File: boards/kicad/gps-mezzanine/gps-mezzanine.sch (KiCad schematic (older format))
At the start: 13 parts, among them P1 CONN_02X20, Q1 BSS138, Q2 BSS138, U1 MCP1700T-3302E/TT, U2 FGPMMOPA6H

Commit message: Update GPS mezzanine
Adds CR2032 backup battery.
Adds uFL external antenna connector.
Connects PPS and fix signal to base board.
Switches to TXS0104 for level translation.

Signed-off-by: Michael Welling <mwelling@ieee.org>
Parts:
- removed Q1, Q2: BSS138, TO_SOT_Packages_SMD:SOT-23, symbol BSS138
- removed R2, R4: 10K, Resistors_SMD:R_0603, symbol R
- added BT1: Battery_Cell, 96boards:BAT-HLD-001, symbol Battery_Cell
- added C4, C5: .1uF, Capacitors_SMD:C_0603, symbol C_Small
- added JK1: uFL, 96boards:U.FL-R-SMT-1, symbol ANTENNA_RCPT
- added MH1, MH2, MH3, MH4: M2.5, Mounting_Holes:MountingHole_2-5mm, symbol MOUNTING_HOLE
- added U3: TXS0104E, Housings_SSOP:SSOP-14_5.3x6.2mm_Pitch0.65mm, symbol TXS0104E
- R1: value 10K -> 1K
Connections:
- net labels added: +BATT, GPS_1PPS
- wire segments 81 -> 92
- no-connect marks 4 -> 2
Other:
- note added: "KIT ACCESSORIES:\n1 - CR2032\n2 - M2102-2545-AL\n2 - M2.5 Screws\n2 - M2.4 Nuts"
- moved on the sheet: C2, C3, U1

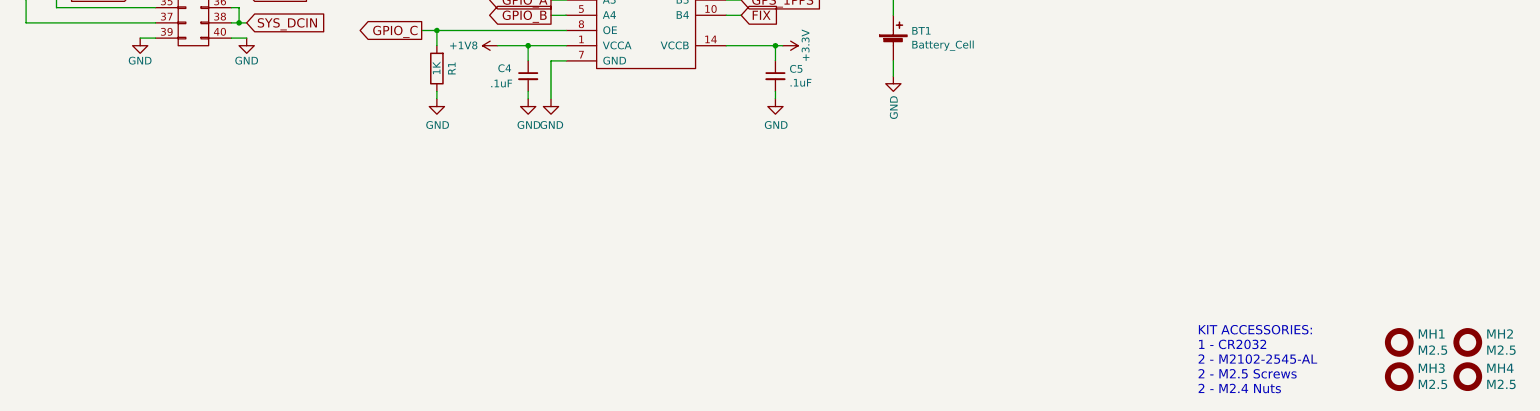
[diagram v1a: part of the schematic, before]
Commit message: Add UART header and schematic PDF
Signed-off-by: Michael Welling <mwelling@ieee.org>
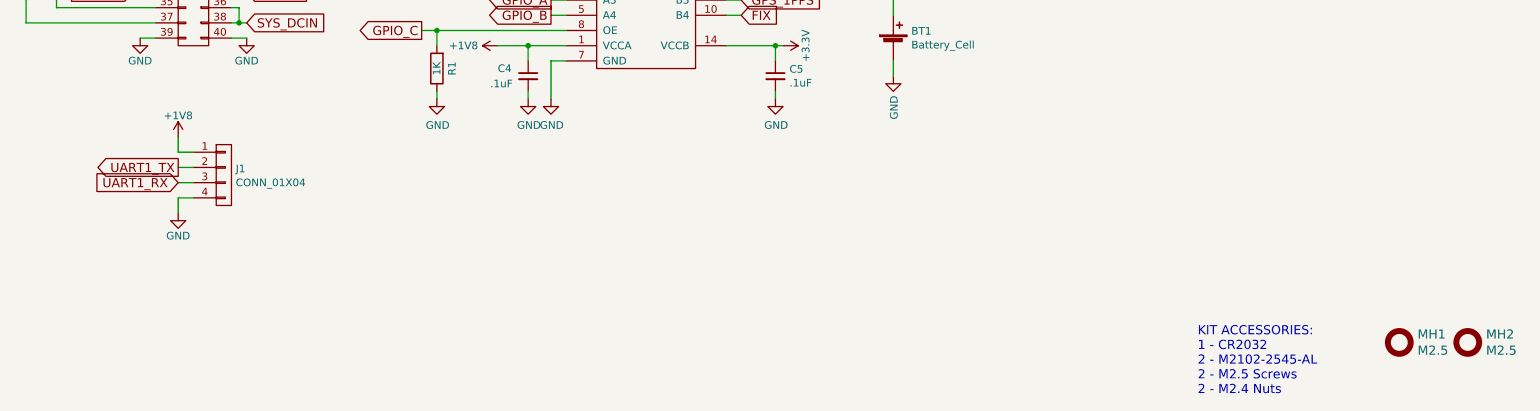
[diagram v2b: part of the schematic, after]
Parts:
- removed MH3, MH4: M2.5, Mounting_Holes:MountingHole_2-5mm, symbol MOUNTING_HOLE
- added J1: CONN_01X04, Pin_Headers:Pin_Header_Straight_1x04, symbol CONN_01X04
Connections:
- net +1V8: now also J1.1 (P1)
- net GND: now also J1.4 (P4)
- net UART1_RX: now also J1.3 (P3)
- net UART1_TX: now also J1.2 (P2)
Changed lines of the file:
@@
-	1    0    0    -1
-$EndComp
-$Comp
-L MOUNTING_HOLE MH3
-U 1 1 5A1BBDB6
-P 10425 6325
-F 0 "MH3" H 10545 6378 60  0000 L CNN
-F 1 "M2.5" H 10545 6272 60  0000 L CNN
-F 2 "Mounting_Holes:MountingHole_2-5mm" H 10425 6325 60  0001 C CNN
-F 3 "" H 10425 6325 60  0001 C CNN
-	1    10425 6325
-	1    0    0    -1
-$EndComp
-$Comp
-L MOUNTING_HOLE MH4
-U 1 1 5A1BBDF8
-P 10875 6325
-F 0 "MH4" H 10995 6378 60  0000 L CNN
-F 1 "M2.5" H 10995 6272 60  0000 L CNN
-F 2 "Mounting_Holes:MountingHole_2-5mm" H 10875 6325 60  0001 C CNN
-F 3 "" H 10875 6325 60  0001 C CNN
-	1    10875 6325
 	1    0    0    -1
 $EndComp
 Text Notes 9100 6450 0    60   ~ 0
 KIT ACCESSORIES:\n1 - CR2032\n2 - M2102-2545-AL\n2 - M2.5 Screws\n2 - M2.4 Nuts
+$Comp
+L GND #PWR030
+U 1 1 5A21B1B9
+P 2400 5250
+F 0 "#PWR030" H 2400 5000 50  0001 C CNN
+F 1 "GND" H 2400 5100 50  0000 C CNN
+F 2 "" H 2400 5250 60  0000 C CNN
+F 3 "" H 2400 5250 60  0000 C CNN
+	1    2400 5250
+	1    0    0    -1
+$EndComp
+Text GLabel 2400 4950 0    60   Output ~ 0
+UART1_TX
+Text GLabel 2400 5050 0    60   Input ~ 0
+UART1_RX
+$Comp
+L CONN_01X04 J1
+U 1 1 5A21B99A
+P 2700 5000
+F 0 "J1" H 2778 5041 50  0000 L CNN
+F 1 "CONN_01X04" H 2778 4950 50  0000 L CNN
+F 2 "Pin_Headers:Pin_Header_Straight_1x04" H 2700 5000 50  0001 C CNN
+F 3 "" H 2700 5000 50  0001 C CNN
+	1    2700 5000
+	1    0    0    -1
+$EndComp
+$Comp
+L +1V8 #PWR029
+U 1 1 5A21BAE7
+P 2400 4750
+F 0 "#PWR029" H 2400 4600 50  0001 C CNN
+F 1 "+1V8" H 2400 4890 50  0000 C CNN
+F 2 "" H 2400 4750 60  0000 C CNN
+F 3 "" H 2400 4750 60  0000 C CNN
+	1    2400 4750
+	1    0    0    -1
+$EndComp
+Wire Wire Line
+	2400 4750 2400 4850
+Wire Wire Line
+	2400 4850 2500 4850
+Wire Wire Line
+	2400 4950 2500 4950
+Wire Wire Line
+	2400 5050 2500 5050
+Wire Wire Line
+	2400 5250 2400 5150
+Wire Wire Line
+	2400 5150 2500 5150
 $EndSCHEMATC

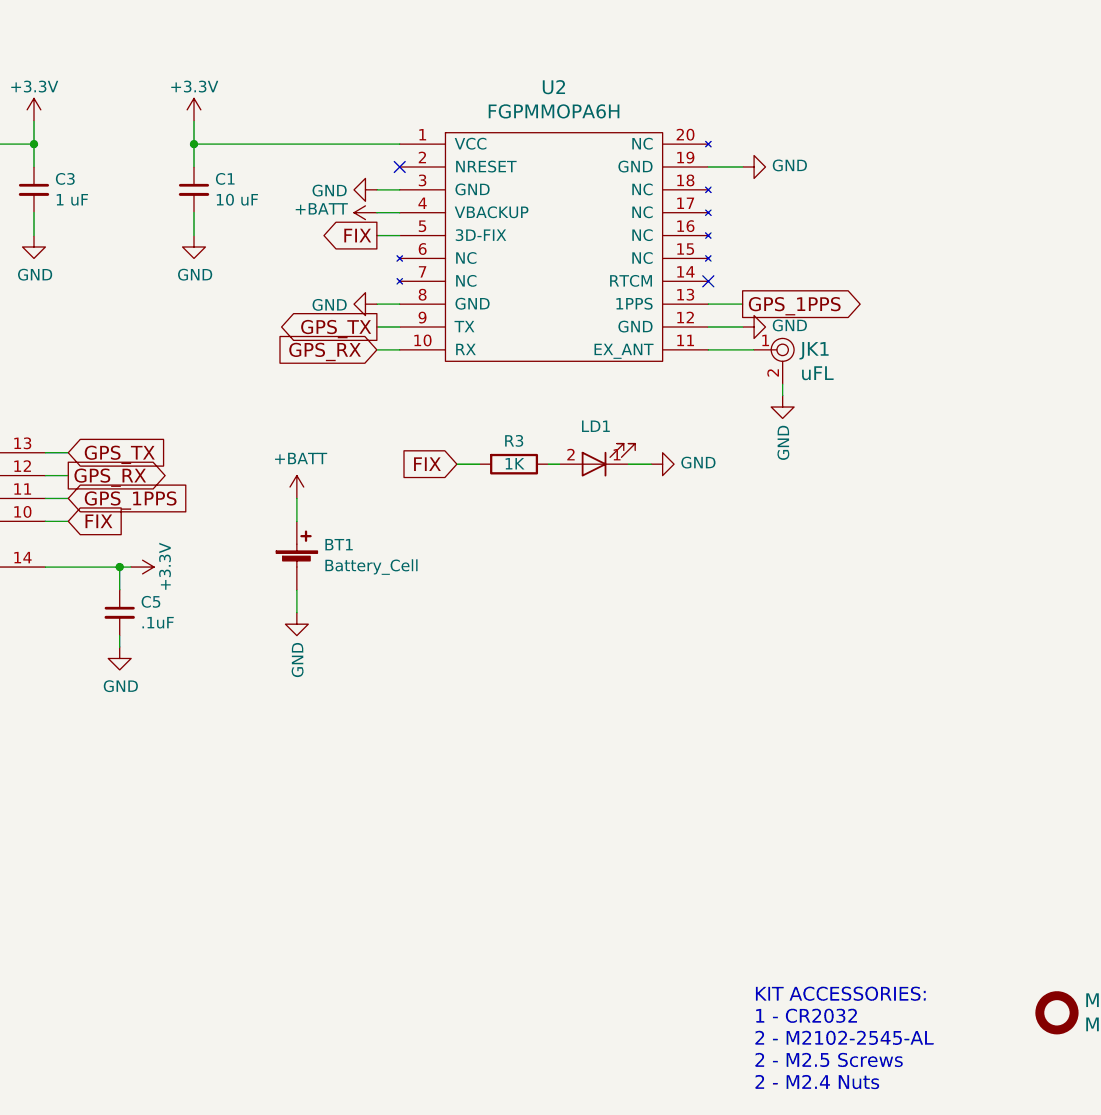
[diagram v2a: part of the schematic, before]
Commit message: Add ferrite bead to GPS power supply
Signed-off-by: Michael Welling <mwelling@ieee.org>
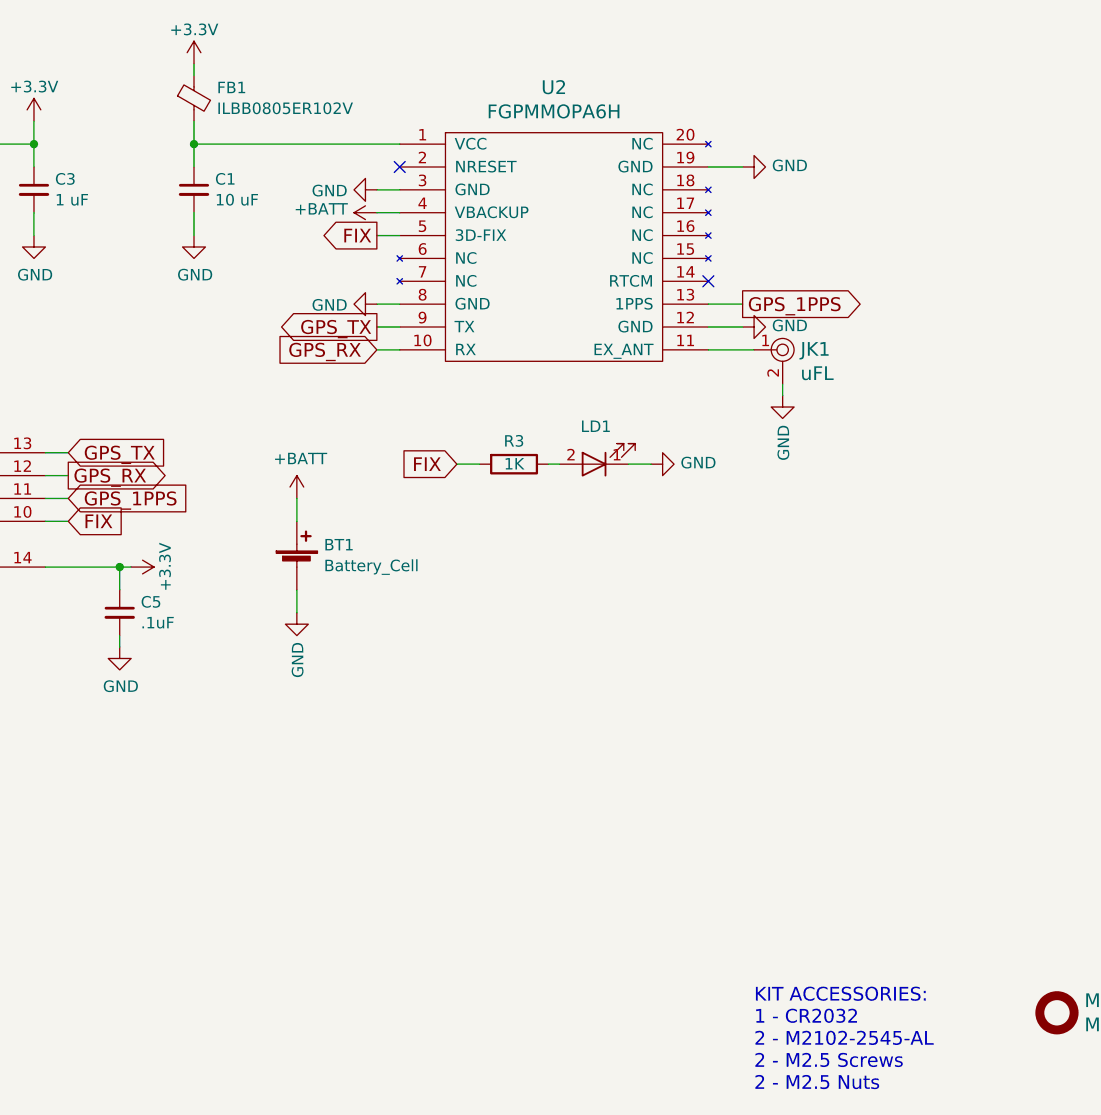
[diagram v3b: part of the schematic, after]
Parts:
- added FB1: ILBB0805ER102V, Resistors_SMD:R_0805_HandSoldering, symbol Ferrite_Bead_Small
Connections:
- net +3V3: now also FB1.1; no longer C1.1, U2.1 (VCC)
- new net: C1.1, FB1.2, U2.1 (VCC)
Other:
- note added: "KIT ACCESSORIES:\n1 - CR2032\n2 - M2102-2545-AL\n2 - M2.5 Screws\n2 - M2.5 Nuts"
- note removed: "KIT ACCESSORIES:\n1 - CR2032\n2 - M2102-2545-AL\n2 - M2.5 Screws\n2 - M2.4 Nuts"
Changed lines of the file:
@@
 L +3.3V #PWR06
 U 1 1 59ACB38D
-P 6650 2200
-F 0 "#PWR06" H 6650 2050 50  0001 C CNN
-F 1 "+3.3V" H 6650 2350 50  0000 C CNN
-F 2 "" H 6650 2200 50  0001 C CNN
-F 3 "" H 6650 2200 50  0001 C CNN
-	1    6650 2200
+P 6650 1950
+F 0 "#PWR06" H 6650 1800 50  0001 C CNN
+F 1 "+3.3V" H 6650 2100 50  0000 C CNN
+F 2 "" H 6650 1950 50  0001 C CNN
+F 3 "" H 6650 1950 50  0001 C CNN
+	1    6650 1950
 	1    0    0    -1
 $EndComp
@@
 $EndComp
 Text Notes 9100 6450 0    60   ~ 0
-KIT ACCESSORIES:\n1 - CR2032\n2 - M2102-2545-AL\n2 - M2.5 Screws\n2 - M2.4 Nuts
+KIT ACCESSORIES:\n1 - CR2032\n2 - M2102-2545-AL\n2 - M2.5 Screws\n2 - M2.5 Nuts
 $Comp
 L GND #PWR030
@@
 Wire Wire Line
 	2400 5150 2500 5150
+$Comp
+L Ferrite_Bead_Small FB1
+U 1 1 5AEDFFA2
+P 6650 2100
+F 0 "FB1" H 6750 2146 50  0000 L CNN
+F 1 "ILBB0805ER102V" H 6750 2055 50  0000 L CNN
+F 2 "Resistors_SMD:R_0805_HandSoldering" V 6580 2100 50  0001 C CNN
+F 3 "" H 6650 2100 50  0001 C CNN
+	1    6650 2100
+	1    0    0    -1
+$EndComp
+Wire Wire Line
+	6650 1950 6650 2000
 $EndSCHEMATC

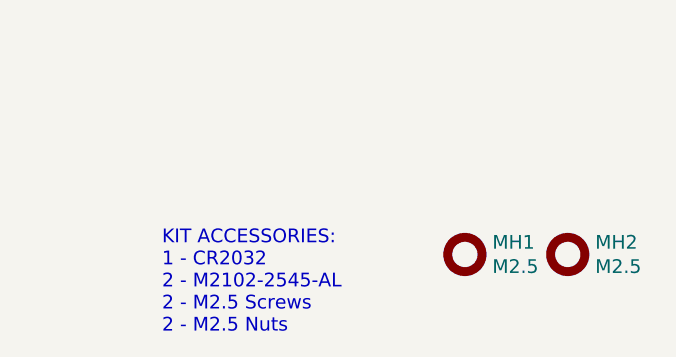
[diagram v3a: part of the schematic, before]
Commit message: Increase board size to full form factor
To make room for prototyping area and possible USB UART.

Signed-off-by: Michael Welling <mwelling@ieee.org>
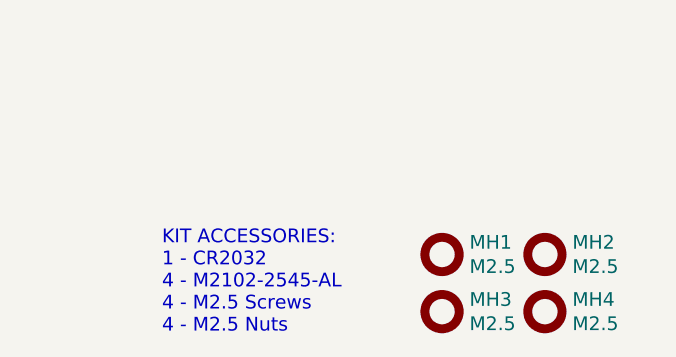
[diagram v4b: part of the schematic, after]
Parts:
- added MH3, MH4: M2.5, Mounting_Holes:MountingHole_2-5mm, symbol MOUNTING_HOLE
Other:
- note added: "KIT ACCESSORIES:\n1 - CR2032\n4 - M2102-2545-AL\n4 - M2.5 Screws\n4 - M2.5 Nuts"
- note removed: "KIT ACCESSORIES:\n1 - CR2032\n2 - M2102-2545-AL\n2 - M2.5 Screws\n2 - M2.5 Nuts"
- moved on the sheet: MH1, MH2
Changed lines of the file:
@@
 L MOUNTING_HOLE MH1
 U 1 1 5A1BBBD1
-P 10425 6100
-F 0 "MH1" H 10545 6153 60  0000 L CNN
-F 1 "M2.5" H 10545 6047 60  0000 L CNN
-F 2 "Mounting_Holes:MountingHole_2-5mm" H 10425 6100 60  0001 C CNN
-F 3 "" H 10425 6100 60  0001 C CNN
-	1    10425 6100
+P 10325 6100
+F 0 "MH1" H 10445 6153 60  0000 L CNN
+F 1 "M2.5" H 10445 6047 60  0000 L CNN
+F 2 "Mounting_Holes:MountingHole_2-5mm" H 10325 6100 60  0001 C CNN
+F 3 "" H 10325 6100 60  0001 C CNN
+	1    10325 6100
 	1    0    0    -1
 $EndComp
@@
 L MOUNTING_HOLE MH2
 U 1 1 5A1BBD7A
-P 10875 6100
-F 0 "MH2" H 10995 6153 60  0000 L CNN
-F 1 "M2.5" H 10995 6047 60  0000 L CNN
-F 2 "Mounting_Holes:MountingHole_2-5mm" H 10875 6100 60  0001 C CNN
-F 3 "" H 10875 6100 60  0001 C CNN
-	1    10875 6100
+P 10775 6100
+F 0 "MH2" H 10895 6153 60  0000 L CNN
+F 1 "M2.5" H 10895 6047 60  0000 L CNN
+F 2 "Mounting_Holes:MountingHole_2-5mm" H 10775 6100 60  0001 C CNN
+F 3 "" H 10775 6100 60  0001 C CNN
+	1    10775 6100
 	1    0    0    -1
 $EndComp
 Text Notes 9100 6450 0    60   ~ 0
-KIT ACCESSORIES:\n1 - CR2032\n2 - M2102-2545-AL\n2 - M2.5 Screws\n2 - M2.5 Nuts
+KIT ACCESSORIES:\n1 - CR2032\n4 - M2102-2545-AL\n4 - M2.5 Screws\n4 - M2.5 Nuts
 $Comp
 L GND #PWR030
@@
 Wire Wire Line
 	6650 1950 6650 2000
+$Comp
+L MOUNTING_HOLE MH3
+U 1 1 5AEE09C6
+P 10325 6350
+F 0 "MH3" H 10445 6403 60  0000 L CNN
+F 1 "M2.5" H 10445 6297 60  0000 L CNN
+F 2 "Mounting_Holes:MountingHole_2-5mm" H 10325 6350 60  0001 C CNN
+F 3 "" H 10325 6350 60  0001 C CNN
+	1    10325 6350
+	1    0    0    -1
+$EndComp
+$Comp
+L MOUNTING_HOLE MH4
+U 1 1 5AEE0A40
+P 10775 6350
+F 0 "MH4" H 10895 6403 60  0000 L CNN
+F 1 "M2.5" H 10895 6297 60  0000 L CNN
+F 2 "Mounting_Holes:MountingHole_2-5mm" H 10775 6350 60  0001 C CNN
+F 3 "" H 10775 6350 60  0001 C CNN
+	1    10775 6350
+	1    0    0    -1
+$EndComp
 $EndSCHEMATC

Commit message: Add headers, proto area, and route
Signed-off-by: Michael Welling <mwelling@ieee.org>
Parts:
- removed J1: CONN_01X04, Pin_Headers:Pin_Header_Straight_1x04, symbol CONN_01X04
- added C10, C9: 1uF, Capacitors_SMD:C_0603, symbol C_Small
- added C11: .1uF, Capacitors_SMD:C_0603, symbol C_Small
- added C6: 4.7uF, Capacitors_SMD:C_0603, symbol C_Small
- added C7, C8: 47pF, Capacitors_SMD:C_0603, symbol C_Small
- added FB2: ILBB0805ER102V, Resistors_SMD:R_0805_HandSoldering, symbol Ferrite_Bead_Small
- added J1: USB_OTG, Connect:USB_Micro-B, symbol USB_OTG
- added J2, J3: CONN_02X06, Pin_Headers:Pin_Header_Straight_2x06, symbol CONN_02X06
- added R2: 10K, Resistors_SMD:R_0603, symbol R
- added R4, R5: 27, Resistors_SMD:R_0603, symbol R
- added R6, R7: 220, Resistors_SMD:R_0603, symbol R
- added U4: FT230X, Housings_SSOP:SSOP-16_3.9x4.9mm_Pitch0.635mm, symbol FT230X
- added U5: MCP1700T-1802E, TO_SOT_Packages_SMD:SOT-23, symbol MCP1700T-1802E
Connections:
- net +1V8: now also J3.5 (P5), J3.6 (P6)
- net +5V: now also J3.7 (P7), J3.8 (P8)
- net GND: now also C10.2, C11.2, C6.2, C7.2, C8.2, C9.2, J1.5 (GND), J1.6 (Shield), J3.10 (P10), J3.11 (P11), J3.12 (P12), J3.9 (P9), U4.13 (GND), U4.5 (GND), U5.1 (GND)
- net GPIO_D: now also J2.10 (P10)
- net GPIO_E: now also J2.9 (P9)
- net GPIO_F: now also J2.12 (P12)
- net GPIO_G: now also J2.11 (P11)
- net GPIO_H: now also J3.2 (P2)
- net GPIO_I: now also J3.1 (P1)
- net GPIO_J: now also J3.4 (P4)
- net GPIO_K: now also J3.3 (P3)
- net I2C0_SCL: now also J2.1 (P1)
- net I2C0_SDA: now also J2.3 (P3)
- net I2C1_SCL: now also J2.5 (P5)
- net I2C1_SDA: now also J2.7 (P7)
- net PWR_BTN_N: now also R6.2
- net RST_BTN_N: now also R7.2
- net SPIO_CS: now also J2.6 (P6)
- net SPIO_DIN: now also J2.4 (P4)
- net SPIO_DOUT: now also J2.8 (P8)
- net SPIO_SCL: now also J2.2 (P2)
- net UART1_RX: now also U4.1 (TXD)
- net UART1_TX: now also U4.4 (RXD)
- new net: C6.1, FB2.1, U4.12 (VCC)
- new net: FB2.2, J1.1 (VBUS)
- new net: C7.1, J1.2 (D-), R5.2
- new net: C8.1, J1.3 (D+), R4.2
- new net: R2.1, U4.11 (RESET#)
- new net: R7.1, U4.16 (CBUS3)
- new net: R6.1, U4.7 (CBUS2)
- new net: R4.1, U4.8 (USBDP)
- new net: R5.1, U4.9 (USBDM)
- new net 1V8U: C10.1, R2.2, U4.3 (VCCIO), U5.2 (VO)
- new net 3P3U: C11.1, C9.1, U4.10 (3V3OUT), U5.3 (VI)
- no-connect marks 2 -> 7
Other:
- note added: "USB SERIAL CONSOLE"
- moved on the sheet: BT1, C1, C2, C3, C4, C5, FB1, JK1, LD1, P1, R1, R3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

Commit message: Add part numbers to various parts to BOM export
Signed-off-by: Michael Welling <mwelling@ieee.org>
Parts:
- BT1: Mfg Part Number (none) -> BAT-HLD-001-TR
- FB1, FB2: Mfg Part Number (none) -> ILBB0805ER102V
- J1: Mfg Part Number (none) -> 10118194-0001LF
- JK1: Mfg Part Number (none) -> U.FL-R-SMT-1
- P1: Mfg Part Number (none) -> 57202-G52-20LF; Mfr Part # P220-1220A0xMxxxx2 -> 57202-G52-20LF
- U1: Mfg Part Number (none) -> MCP1700T-3302E/TT
- U2: Mfg Part Number (none) -> FGPMMOPA6H
- U3: Mfg Part Number (none) -> TXS0104EPWR
- U4: Mfg Part Number (none) -> FT230XS-R
- U5: Mfg Part Number (none) -> MCP1700T-1802E/TT
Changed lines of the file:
@@
 F 2 "96boards:Pin_Header_SMD_2x20_Pitch2mm" H 2900 1825 60  0001 C CNN
 F 3 "" H 2900 1825 60  0000 C CNN
-F 4 "Yxcon" H 2900 2775 60  0001 C CNN "Mfr"
-F 5 "P220-1220A0xMxxxx2" H 2900 2775 60  0001 C CNN "Mfr Part #"
+F 4 "57202-G52-20LF" H 2900 2775 60  0001 C CNN "Mfg Part Number"
+F 5 "Yxcon" H 2900 2775 60  0001 C CNN "Mfr"
+F 6 "57202-G52-20LF" H 2900 2775 60  0001 C CNN "Mfr Part #"
 	1    2900 2775
 	1    0    0    -1
@@
 F 2 "TO_SOT_Packages_SMD:SOT-23" H 5750 2125 50  0001 C CNN
 F 3 "" H 5750 2125 50  0001 C CNN
+F 4 "MCP1700T-3302E/TT" H 5750 2025 60  0001 C CNN "Mfg Part Number"
 	1    5750 2025
 	1    0    0    -1
@@
 F 2 "96boards:FGPMMOPA6H" H 8600 2425 60  0001 C CNN
 F 3 "" H 8600 2425 60  0001 C CNN
+F 4 "FGPMMOPA6H" H 8600 2425 60  0001 C CNN "Mfg Part Number"
 	1    8600 2425
 	1    0    0    -1
@@
 F 2 "96boards:BAT-HLD-001" V 7500 3660 50  0001 C CNN
 F 3 "" V 7500 3660 50  0001 C CNN
+F 4 "BAT-HLD-001-TR" H 7500 3600 60  0001 C CNN "Mfg Part Number"
 	1    7500 3600
 	1    0    0    -1
@@
 F 2 "Housings_SSOP:SSOP-14_5.3x6.2mm_Pitch0.65mm" H 5550 3175 60  0001 C CNN
 F 3 "" H 5550 3175 60  0001 C CNN
+F 4 "TXS0104EPWR" H 5900 3175 60  0001 C CNN "Mfg Part Number"
 	1    5900 3175
 	1    0    0    -1
@@
 F 2 "96boards:U.FL-R-SMT-1" H 9625 2825 60  0001 C CNN
 F 3 "" H 9625 2825 60  0001 C CNN
+F 4 "U.FL-R-SMT-1" H 9625 2825 60  0001 C CNN "Mfg Part Number"
 	1    9625 2825
 	1    0    0    -1
@@
 F 2 "Resistors_SMD:R_0805_HandSoldering" V 6980 1725 50  0001 C CNN
 F 3 "" H 7050 1725 50  0001 C CNN
+F 4 "ILBB0805ER102V" H 7050 1725 60  0001 C CNN "Mfg Part Number"
 	1    7050 1725
 	1    0    0    -1
@@
 F 2 "Housings_SSOP:SSOP-16_3.9x4.9mm_Pitch0.635mm" H 5750 5375 60  0001 C CNN
 F 3 "" H 5750 5375 60  0000 C CNN
+F 4 "FT230XS-R" H 5750 5375 60  0001 C CNN "Mfg Part Number"
 	1    5750 5375
 	1    0    0    -1
@@
 F 2 "TO_SOT_Packages_SMD:SOT-23" H 8575 5225 40  0001 C CNN
 F 3 "" H 8575 5125 60  0000 C CNN
+F 4 "MCP1700T-1802E/TT" H 8575 5125 60  0001 C CNN "Mfg Part Number"
 	1    8575 5125
 	1    0    0    -1
@@
 F 2 "Resistors_SMD:R_0805_HandSoldering" V 3880 4875 50  0001 C CNN
 F 3 "" H 3950 4875 50  0001 C CNN
+F 4 "ILBB0805ER102V" H 3950 4875 60  0001 C CNN "Mfg Part Number"
 	1    3950 4875
 	0    1    1    0
@@
 F 2 "Connect:USB_Micro-B" H 3550 5025 50  0001 C CNN
 F 3 "" H 3550 5025 50  0001 C CNN
+F 4 "10118194-0001LF" H 3400 5075 60  0001 C CNN "Mfg Part Number"
 	1    3400 5075
 	1    0    0    -1
@@
 Connection ~ 6175 7100
 $Comp
-L +1V8 #PWR?
+L +1V8 #PWR042
 U 1 1 5AF1F297
 P 6675 6725
-F 0 "#PWR?" H 6675 6575 50  0001 C CNN
+F 0 "#PWR042" H 6675 6575 50  0001 C CNN
 F 1 "+1V8" H 6675 6865 50  0000 C CNN
 F 2 "" H 6675 6725 60  0000 C CNN
@@
 $EndComp
 $Comp
-L +5V #PWR?
+L +5V #PWR043
 U 1 1 5AF1F2EA
 P 6875 6725
-F 0 "#PWR?" H 6875 6575 50  0001 C CNN
+F 0 "#PWR043" H 6875 6575 50  0001 C CNN
 F 1 "+5V" H 6875 6865 50  0000 C CNN
 F 2 "" H 6875 6725 60  0000 C CNN
